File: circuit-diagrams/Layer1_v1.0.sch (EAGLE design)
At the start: 41 parts, among them U1 MCP73831, X1 USBSMD

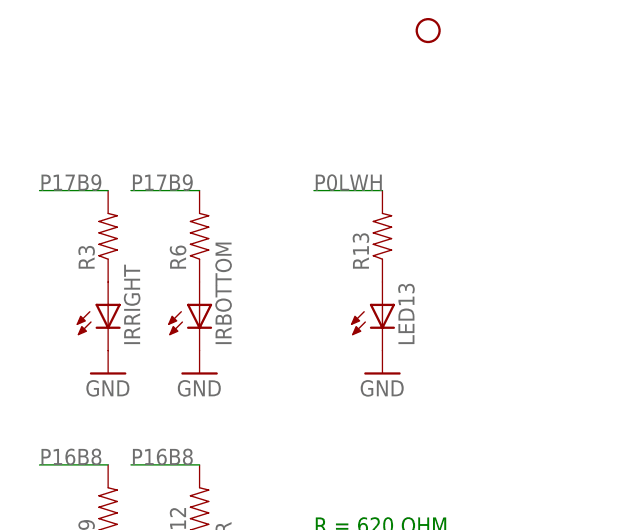
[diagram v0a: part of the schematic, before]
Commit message: Fixed mapping of pins in layer 2 in v1.1
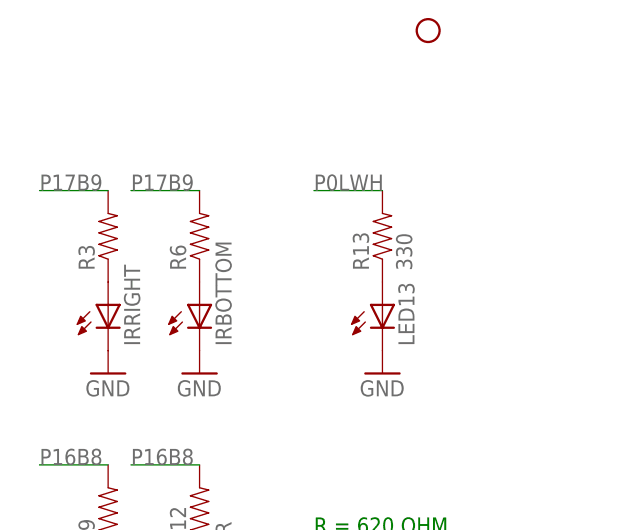
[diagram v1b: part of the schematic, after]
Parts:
- R13: value (none) -> 330
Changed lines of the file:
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@@
 <grid distance="0.1" unitdist="inch" unit="inch" style="lines" multiple="1" display="no" altdistance="0.01" altunitdist="inch" altunit="inch"/>
 <layers>
-<layer number="1" name="Top" color="4" fill="1" visible="yes" active="no"/>
-<layer number="16" name="Bottom" color="1" fill="1" visible="yes" active="no"/>
-<layer number="17" name="Pads" color="2" fill="1" visible="yes" active="no"/>
-<layer number="18" name="Vias" color="2" fill="1" visible="yes" active="no"/>
-<layer number="19" name="Unrouted" color="6" fill="1" visible="yes" active="no"/>
-<layer number="20" name="Dimension" color="15" fill="1" visible="yes" active="no"/>
-<layer number="21" name="tPlace" color="7" fill="1" visible="yes" active="no"/>
-<layer number="22" name="bPlace" color="7" fill="1" visible="yes" active="no"/>
-<layer number="23" name="tOrigins" color="15" fill="1" visible="yes" active="no"/>
-<layer number="24" name="bOrigins" color="15" fill="1" visible="yes" active="no"/>
-<layer number="25" name="tNames" color="7" fill="1" visible="yes" active="no"/>
-<layer number="26" name="bNames" color="7" fill="1" visible="yes" active="no"/>
-<layer number="27" name="tValues" color="7" fill="1" visible="yes" active="no"/>
-<layer number="28" name="bValues" color="7" fill="1" visible="yes" active="no"/>
+<layer number="1" name="Top" color="4" fill="1" visible="no" active="no"/>
+<layer number="16" name="Bottom" color="1" fill="1" visible="no" active="no"/>
+<layer number="17" name="Pads" color="2" fill="1" visible="no" active="no"/>
+<layer number="18" name="Vias" color="2" fill="1" visible="no" active="no"/>
+<layer number="19" name="Unrouted" color="6" fill="1" visible="no" active="no"/>
+<layer number="20" name="Dimension" color="15" fill="1" visible="no" active="no"/>
+<layer number="21" name="tPlace" color="7" fill="1" visible="no" active="no"/>
+<layer number="22" name="bPlace" color="7" fill="1" visible="no" active="no"/>
+<layer number="23" name="tOrigins" color="15" fill="1" visible="no" active="no"/>
+<layer number="24" name="bOrigins" color="15" fill="1" visible="no" active="no"/>
+<layer number="25" name="tNames" color="7" fill="1" visible="no" active="no"/>
+<layer number="26" name="bNames" color="7" fill="1" visible="no" active="no"/>
+<layer number="27" name="tValues" color="7" fill="1" visible="no" active="no"/>
+<layer number="28" name="bValues" color="7" fill="1" visible="no" active="no"/>
 <layer number="29" name="tStop" color="7" fill="3" visible="no" active="no"/>
 <layer number="30" name="bStop" color="7" fill="6" visible="no" active="no"/>
@@
 <layer number="35" name="tGlue" color="7" fill="4" visible="no" active="no"/>
 <layer number="36" name="bGlue" color="7" fill="5" visible="no" active="no"/>
-<layer number="37" name="tTest" color="7" fill="1" visible="yes" active="no"/>
-<layer number="38" name="bTest" color="7" fill="1" visible="yes" active="no"/>
+<layer number="37" name="tTest" color="7" fill="1" visible="no" active="no"/>
+<layer number="38" name="bTest" color="7" fill="1" visible="no" active="no"/>
 <layer number="39" name="tKeepout" color="4" fill="11" visible="no" active="no"/>
 <layer number="40" name="bKeepout" color="1" fill="11" visible="no" active="no"/>
@@
 <layer number="44" name="Drills" color="7" fill="1" visible="no" active="no"/>
 <layer number="45" name="Holes" color="7" fill="1" visible="no" active="no"/>
-<layer number="46" name="Milling" color="3" fill="1" visible="yes" active="no"/>
-<layer number="47" name="Measures" color="7" fill="1" visible="yes" active="no"/>
-<layer number="48" name="Document" color="7" fill="1" visible="yes" active="no"/>
-<layer number="49" name="Reference" color="7" fill="1" visible="yes" active="no"/>
-<layer number="50" name="dxf" color="7" fill="1" visible="yes" active="no"/>
-<layer number="51" name="tDocu" color="7" fill="1" visible="yes" active="no"/>
-<layer number="52" name="bDocu" color="7" fill="1" visible="yes" active="no"/>
-<layer number="53" name="tGND_GNDA" color="7" fill="9" visible="yes" active="no"/>
-<layer number="54" name="bGND_GNDA" color="1" fill="9" visible="yes" active="no"/>
-<layer number="56" name="wert" color="7" fill="1" visible="yes" active="no"/>
+<layer number="46" name="Milling" color="3" fill="1" visible="no" active="no"/>
+<layer number="47" name="Measures" color="7" fill="1" visible="no" active="no"/>
+<layer number="48" name="Document" color="7" fill="1" visible="no" active="no"/>
+<layer number="49" name="Reference" color="7" fill="1" visible="no" active="no"/>
+<layer number="50" name="dxf" color="7" fill="1" visible="no" active="no"/>
+<layer number="51" name="tDocu" color="7" fill="1" visible="no" active="no"/>
+<layer number="52" name="bDocu" color="7" fill="1" visible="no" active="no"/>
+<layer number="53" name="tGND_GNDA" color="7" fill="9" visible="no" active="no"/>
+<layer number="54" name="bGND_GNDA" color="1" fill="9" visible="no" active="no"/>
+<layer number="56" name="wert" color="7" fill="1" visible="no" active="no"/>
 <layer number="91" name="Nets" color="2" fill="1" visible="yes" active="yes"/>
 <layer number="92" name="Busses" color="1" fill="1" visible="yes" active="yes"/>
@@
 <part name="GND13" library="SparkFun-Aesthetics" deviceset="GND" device=""/>
 <part name="GND14" library="SparkFun-Aesthetics" deviceset="GND" device=""/>
-<part name="R13" library="SparkFun-Passives" deviceset="RESISTOR" device="0603-RES"/>
+<part name="R13" library="SparkFun-Passives" deviceset="RESISTOR" device="0603-RES" value="330"/>
 <part name="LED13" library="adafruit" deviceset="LED" device="CHIPLED_0603"/>
 <part name="U1" library="SparkFun-PowerIC" deviceset="MCP73831" device=""/>
